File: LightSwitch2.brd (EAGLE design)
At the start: 22 x 44 mm, 5 parts, among them SW1 SWITCH-SPST-ILLUMINATED, SW2 SWITCH-SPST-ILLUMINATED

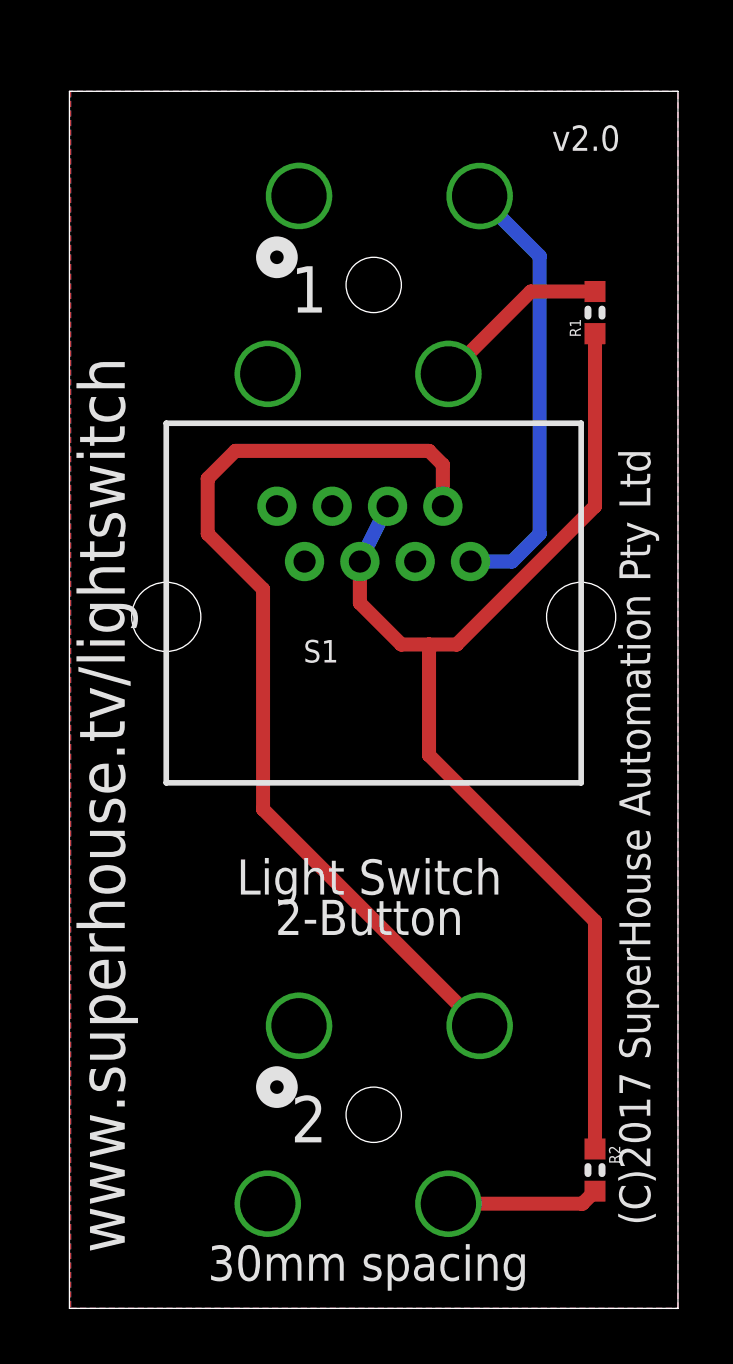
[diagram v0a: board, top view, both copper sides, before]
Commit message: Updated button and RJ45 socket footprints for v2.2
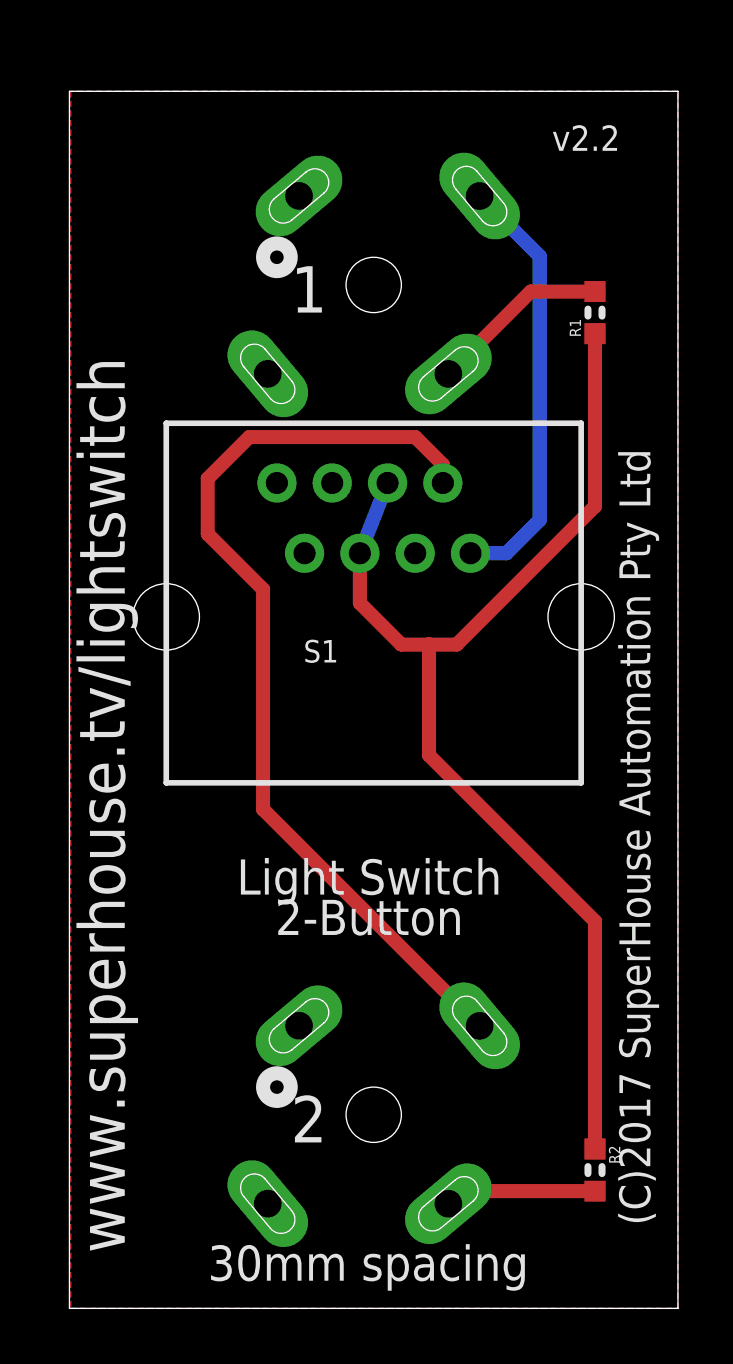
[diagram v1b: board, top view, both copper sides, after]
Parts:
- R1, R2: value 3K3 -> 4K7
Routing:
- net +12V: track 41.9 -> 42.7 mm
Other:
- board text added: "v2.2"
- board text removed: "v2.0"
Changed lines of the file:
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@@
 <?xml version="1.0" encoding="utf-8"?>
 <!DOCTYPE eagle SYSTEM "eagle.dtd">
-<eagle version="8.3.2">
+<eagle version="8.7.0">
 <drawing>
 <settings>
-<setting alwaysvectorfont="yes"/>
+<setting alwaysvectorfont="no"/>
 <setting keepoldvectorfont="yes"/>
 <setting verticaltext="up"/>
@@
 <layer number="60" name="p_dimension" color="6" fill="0" visible="no" active="no"/>
 <layer number="61" name="pt_docu" color="7" fill="0" visible="no" active="no"/>
+<layer number="88" name="SimResults" color="9" fill="1" visible="no" active="no"/>
+<layer number="89" name="SimProbes" color="9" fill="1" visible="no" active="no"/>
 <layer number="90" name="Modules" color="7" fill="1" visible="no" active="no"/>
 <layer number="91" name="Nets" color="2" fill="1" visible="no" active="no"/>
@@
 <wire x1="22" y1="44" x2="22" y2="0" width="0" layer="20"/>
 <text x="21" y="3" size="1.1176" layer="21" font="vector" ratio="15" rot="R90">(C)2017 SuperHouse Automation Pty Ltd</text>
-<text x="17.4452" y="41.8486" size="0.9144" layer="21" font="vector" ratio="15">v2.0</text>
+<text x="17.4452" y="41.8486" size="0.9144" layer="21" font="vector" ratio="15">v2.2</text>
 <text x="10.8412" y="14.8646" size="1.27" layer="21" font="vector" ratio="15" distance="15" align="center">Light Switch
 2-Button</text>
-<text x="2" y="2" size="1.6764" layer="21" ratio="15" rot="R90">www.superhouse.tv/lightswitch</text>
-<text x="8" y="36" size="1.6764" layer="21" ratio="15">1</text>
-<text x="8" y="6" size="1.6764" layer="21" ratio="15">2</text>
-<text x="5" y="1" size="1.27" layer="21" ratio="15">30mm spacing</text>
+<text x="2" y="2" size="1.6764" layer="21" font="vector" ratio="15" rot="R90">www.superhouse.tv/lightswitch</text>
+<text x="8" y="36" size="1.6764" layer="21" font="vector" ratio="15">1</text>
+<text x="8" y="6" size="1.6764" layer="21" font="vector" ratio="15">2</text>
+<text x="5" y="1" size="1.27" layer="21" font="vector" ratio="15">30mm spacing</text>
 <hole x="11" y="37" drill="2"/>
 <hole x="11" y="7" drill="2"/>
@@
 <param name="dpMaxLengthDifference" value="10mm"/>
 <param name="dpGapFactor" value="2.5"/>
-<param name="checkGrid" value="0"/>
 <param name="checkAngle" value="0"/>
 <param name="checkFont" value="1"/>
 <param name="checkRestrict" value="1"/>
+<param name="checkStop" value="0"/>
+<param name="checkValues" value="0"/>
 <param name="useDiameter" value="13"/>
 <param name="maxErrors" value="50"/>
@@
 <element name="SW1" library="freetronics-jon" package="SWITCH-SPST-ILLUMINATED" value="SWITCH-SPST-ILLUMINATED" x="11" y="37" rot="MR50"/>
 <element name="SW2" library="freetronics-jon" package="SWITCH-SPST-ILLUMINATED" value="SWITCH-SPST-ILLUMINATED" x="11" y="7" rot="MR50"/>
-<element name="R1" library="freetronics-jon" package="0603" value="3K3" x="19" y="36" rot="R90"/>
-<element name="R2" library="freetronics-jon" package="0603" value="3K3" x="19" y="5" rot="R270"/>
+<element name="R1" library="freetronics-jon" package="0603" value="4K7" x="19" y="36" rot="R90"/>
+<element name="R2" library="freetronics-jon" package="0603" value="4K7" x="19" y="5" rot="R270"/>
 </elements>
 <signals>
@@
 <contactref element="S1" pad="5"/>
 <contactref element="S1" pad="4"/>
-<wire x1="10.5" y1="27" x2="11.5" y2="29" width="0.508" layer="16"/>
+<wire x1="10.5" y1="27.3" x2="11.5" y2="29.84" width="0.508" layer="16"/>
 <contactref element="R1" pad="1"/>
 <contactref element="R2" pad="1"/>
@@
 <wire x1="13" y1="24" x2="12" y2="24" width="0.508" layer="1"/>
 <wire x1="12" y1="24" x2="10.5" y2="25.5" width="0.508" layer="1"/>
-<wire x1="10.5" y1="25.5" x2="10.5" y2="27" width="0.508" layer="1"/>
+<wire x1="10.5" y1="25.5" x2="10.5" y2="27.3" width="0.508" layer="1"/>
 <wire x1="19" y1="14" x2="13" y2="20" width="0.508" layer="1"/>
 <wire x1="13" y1="20" x2="13" y2="24" width="0.508" layer="1"/>
@@
 <contactref element="S1" pad="1"/>
 <contactref element="SW1" pad="3"/>
-<wire x1="14.5" y1="27" x2="16" y2="27" width="0.508" layer="16"/>
-<wire x1="16" y1="27" x2="17" y2="28" width="0.508" layer="16"/>
-<wire x1="17" y1="28" x2="17" y2="38.0441625" width="0.508" layer="16"/>
-<wire x1="17" y1="38.0441625" x2="14.830225" y2="40.2139375" width="0.508" layer="16"/>
+<wire x1="14.830225" y1="40.2139375" x2="17" y2="38.0441625" width="0.508" layer="16"/>
+<wire x1="17" y1="28.5" x2="15.8" y2="27.3" width="0.508" layer="16"/>
+<wire x1="15.8" y1="27.3" x2="14.5" y2="27.3" width="0.508" layer="16"/>
+<wire x1="17" y1="38.0441625" x2="17" y2="28.5" width="0.508" layer="16"/>
 </signal>
 <signal name="N$5">
 <contactref element="S1" pad="2"/>
-<wire x1="13.5" y1="29" x2="13.5" y2="30.5" width="0.508" layer="1"/>
-<wire x1="13.5" y1="30.5" x2="13" y2="31" width="0.508" layer="1"/>
-<wire x1="13" y1="31" x2="6" y2="31" width="0.508" layer="1"/>
-<wire x1="6" y1="31" x2="5" y2="30" width="0.508" layer="1"/>
+<wire x1="13.5" y1="29.84" x2="13.5" y2="30.5" width="0.508" layer="1"/>
 <wire x1="5" y1="30" x2="5" y2="28" width="0.508" layer="1"/>
 <wire x1="5" y1="28" x2="7" y2="26" width="0.508" layer="1"/>
@@
 <wire x1="7" y1="18.0441625" x2="14.830225" y2="10.2139375" width="0.508" layer="1"/>
 <wire x1="7" y1="26" x2="7" y2="18.0441625" width="0.508" layer="1"/>
+<wire x1="13.5" y1="30.5" x2="12.5" y2="31.5" width="0.508" layer="1"/>
+<wire x1="12.5" y1="31.5" x2="6.5" y2="31.5" width="0.508" layer="1"/>
+<wire x1="6.5" y1="31.5" x2="5" y2="30" width="0.508" layer="1"/>
 </signal>
 <signal name="N$1">
 <contactref element="SW1" pad="2"/>
 <contactref element="R1" pad="2"/>
-<wire x1="13.699709375" y1="33.7826125" x2="16.679096875" y2="36.762" width="0.508" layer="1"/>
-<wire x1="16.679096875" y1="36.762" x2="19" y2="36.762" width="0.508" layer="1"/>
+<wire x1="19" y1="36.762" x2="17" y2="36.762" width="0.508" layer="1"/>
+<wire x1="17" y1="36.762" x2="16.679096875" y2="36.762" width="0.508" layer="1"/>
+<wire x1="16.679096875" y1="36.762" x2="13.699709375" y2="33.7826125" width="0.508" layer="1"/>
 </signal>
 <signal name="N$2">
 <contactref element="SW2" pad="2"/>
 <contactref element="R2" pad="2"/>
-<wire x1="19" y1="4.238" x2="18.5446125" y2="3.7826125" width="0.508" layer="1"/>
-<wire x1="18.5446125" y1="3.7826125" x2="13.699709375" y2="3.7826125" width="0.508" layer="1"/>
+<wire x1="19" y1="4.238" x2="14.155096875" y2="4.238" width="0.508" layer="1"/>
+<wire x1="14.155096875" y1="4.238" x2="13.699709375" y2="3.7826125" width="0.508" layer="1"/>
 </signal>
 </signals>
-<errors>
-</errors>
 </board>
 </drawing>

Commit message: RJ45 footprint change for v2.3
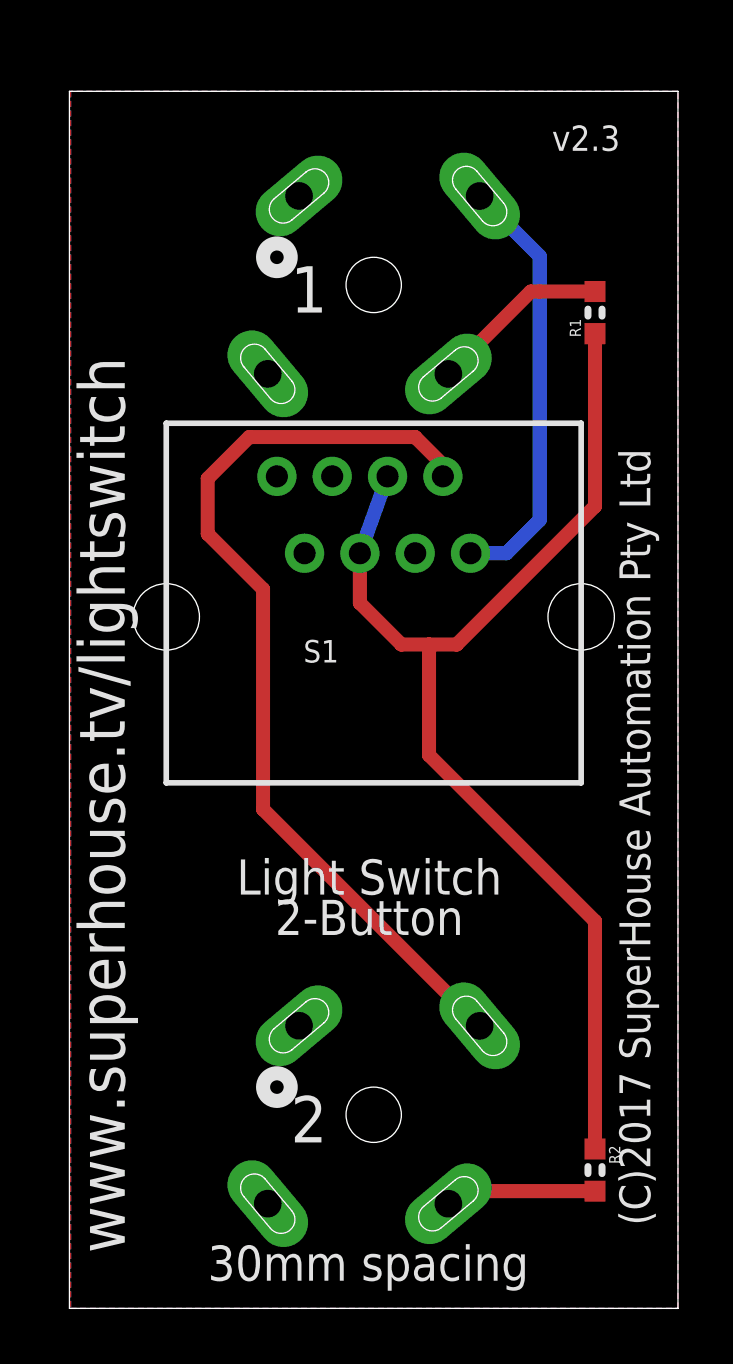
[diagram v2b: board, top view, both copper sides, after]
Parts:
- S1: value RJ45 -> RJ45CH; device freetronics-jon:RJ45 -> freetronics-jon:RJ45CH
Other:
- board text added: "v2.3"
- board text removed: "v2.2"
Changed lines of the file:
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@@
 <?xml version="1.0" encoding="utf-8"?>
 <!DOCTYPE eagle SYSTEM "eagle.dtd">
-<eagle version="8.7.0">
+<eagle version="9.0.0">
 <drawing>
 <settings>
-<setting alwaysvectorfont="no"/>
+<setting alwaysvectorfont="yes"/>
 <setting keepoldvectorfont="yes"/>
 <setting verticaltext="up"/>
@@
 <wire x1="22" y1="44" x2="22" y2="0" width="0" layer="20"/>
 <text x="21" y="3" size="1.1176" layer="21" font="vector" ratio="15" rot="R90">(C)2017 SuperHouse Automation Pty Ltd</text>
-<text x="17.4452" y="41.8486" size="0.9144" layer="21" font="vector" ratio="15">v2.2</text>
+<text x="17.4452" y="41.8486" size="0.9144" layer="21" font="vector" ratio="15">v2.3</text>
 <text x="10.8412" y="14.8646" size="1.27" layer="21" font="vector" ratio="15" distance="15" align="center">Light Switch
 2-Button</text>
@@
 </autorouter>
 <elements>
-<element name="S1" library="freetronics-jon" package="RJ45" value="RJ45" x="11" y="25"/>
+<element name="S1" library="freetronics-jon" package="RJ45CH" value="RJ45CH" x="11" y="25"/>
 <element name="SW1" library="freetronics-jon" package="SWITCH-SPST-ILLUMINATED" value="SWITCH-SPST-ILLUMINATED" x="11" y="37" rot="MR50"/>
 <element name="SW2" library="freetronics-jon" package="SWITCH-SPST-ILLUMINATED" value="SWITCH-SPST-ILLUMINATED" x="11" y="7" rot="MR50"/>
@@
 <contactref element="S1" pad="5"/>
 <contactref element="S1" pad="4"/>
-<wire x1="10.5" y1="27.3" x2="11.5" y2="29.84" width="0.508" layer="16"/>
+<wire x1="10.5" y1="27.3" x2="11.5" y2="30.08" width="0.508" layer="16"/>
 <contactref element="R1" pad="1"/>
 <contactref element="R2" pad="1"/>
@@
 <signal name="N$5">
 <contactref element="S1" pad="2"/>
-<wire x1="13.5" y1="29.84" x2="13.5" y2="30.5" width="0.508" layer="1"/>
+<wire x1="13.5" y1="30.08" x2="13.5" y2="30.5" width="0.508" layer="1"/>
 <wire x1="5" y1="30" x2="5" y2="28" width="0.508" layer="1"/>
 <wire x1="5" y1="28" x2="7" y2="26" width="0.508" layer="1"/>
